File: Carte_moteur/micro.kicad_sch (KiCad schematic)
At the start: 27 parts, among them U501 STM32G474RETx

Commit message: updated motor PCB
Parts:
- removed C501, C507: C, Capacitor_SMD:C_0603_1608Metric_Pad1.08x0.95mm_HandSolder, symbol Device:C
- removed C502: C, Capacitor_SMD:C_0805_2012Metric_Pad1.18x1.45mm_HandSolder, symbol Device:C
- removed R501, R502, R503, R504, R505, R506, R507, R508, R509: R_US, Resistor_SMD:R_0603_1608Metric_Pad0.98x0.95mm_HandSolder, symbol Device:R_US
- added C508: C, Capacitor_SMD:C_0603_1608Metric_Pad1.08x0.95mm_HandSolder, symbol Device:C
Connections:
- net DIR1: now also U501.41 (PC9); no longer U501.43 (PA9)
- net DIR2: now also U501.37 (PB15); no longer U501.45 (PA11)
- net DIR3: now also U501.45 (PA11); no longer U501.41 (PC9)
- net ENC1_A: now also U501.12 (PA0); no longer U501.8 (PC0)
- net ENC1_B: now also U501.13 (PA1); no longer U501.9 (PC1)
- net ENC1_I: now also U501.34 (PB12); no longer U501.46 (PA12)
- net ENC2_A: now also U501.8 (PC0); no longer U501.38 (PC6)
- net ENC2_B: now also U501.9 (PC1); no longer U501.18 (PA4)
- net ENC2_I: now also U501.46 (PA12); no longer U501.55 (PD2)
- net ENC3_A: now also U501.38 (PC6); no longer U501.12 (PA0)
- net ENC3_B: now also U501.18 (PA4); no longer U501.13 (PA1)
- net ENC3_I: now also U501.55 (PD2); no longer U501.34 (PB12)
- net GND: now also C508.1
- net STEP1: now also U501.40 (PC8); no longer U501.42 (PA8)
- net STEP2: now also U501.36 (PB14); no longer U501.44 (PA10)
- net STEP3: now also U501.44 (PA10); no longer U501.40 (PC8)
- net TMC1: now also R514.1, R515.1; no longer R512.1, R513.1
- net TMC2: now also R512.1, R513.1; no longer R516.1, R517.1
- net TMC3: now also R516.1, R517.1; no longer R514.1, R515.1
- net UART3_TX: now also U501.62 (PB9); no longer U501.30 (PB10)
- net at R511.1, U501.28 (VREF+): now also C508.2
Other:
- moved on the sheet: R512, R513, R514, R515, R516, R517

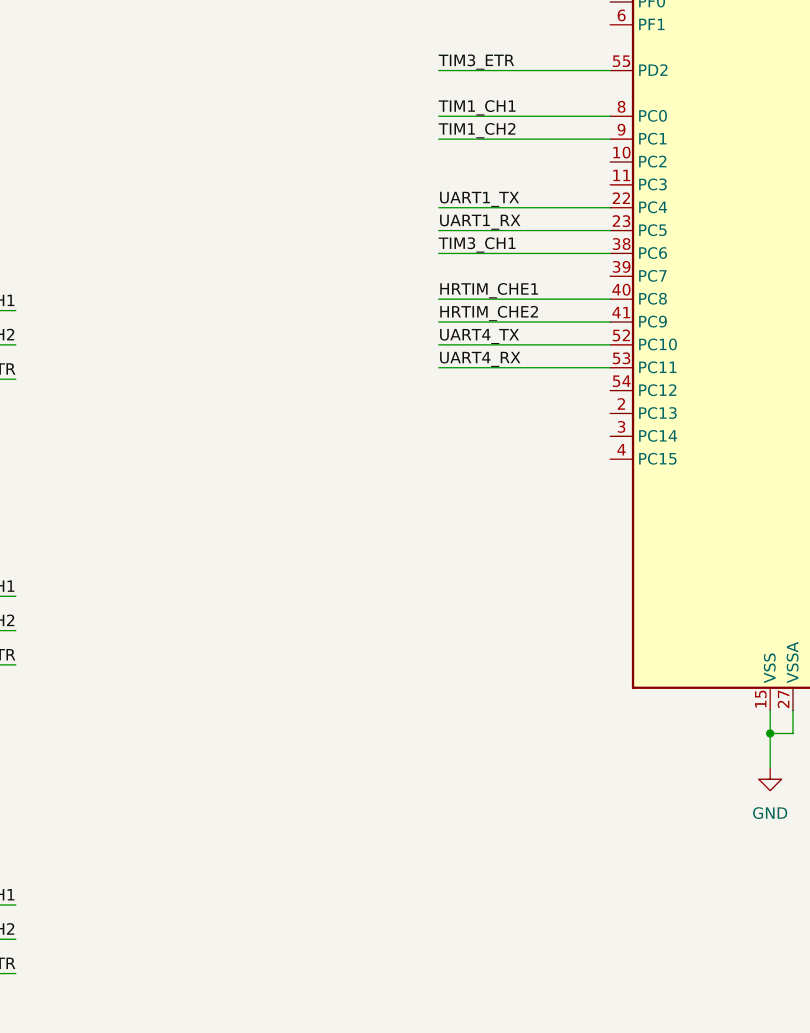
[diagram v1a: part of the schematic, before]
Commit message: debug led added. Modified power connector
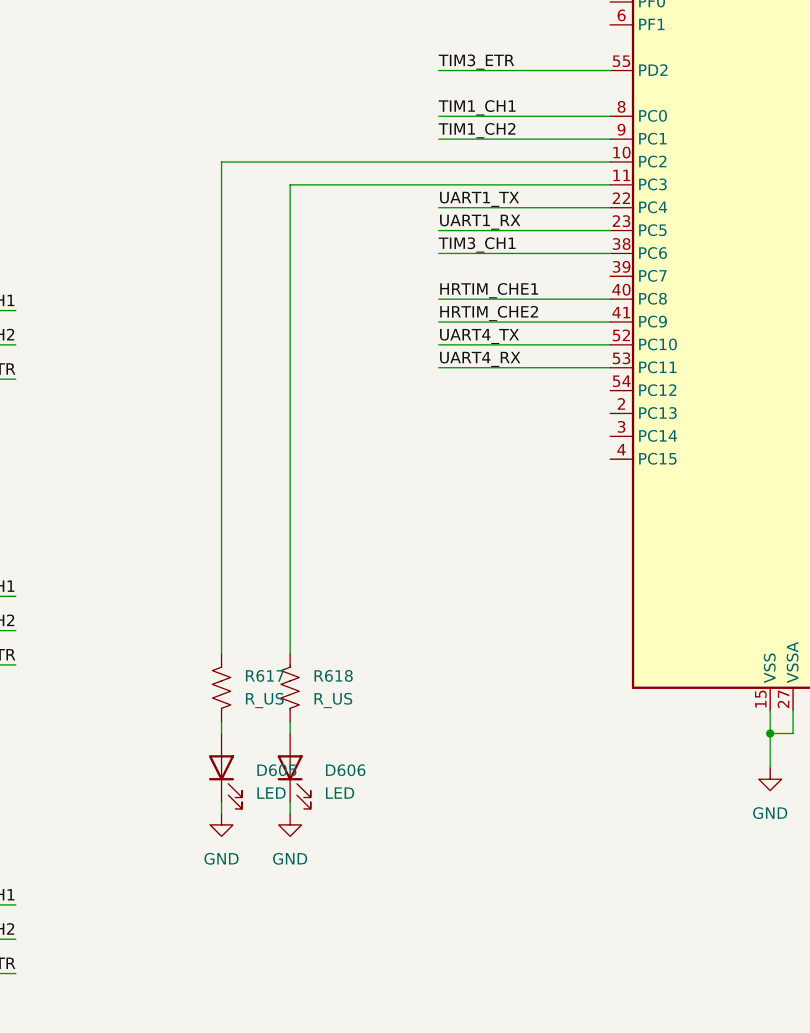
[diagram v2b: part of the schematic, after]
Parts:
- added D605, D606: LED, LED_SMD:LED_0805_2012Metric_Pad1.15x1.40mm_HandSolder, symbol Device:LED
- added R617, R618: R_US, Resistor_SMD:R_0603_1608Metric_Pad0.98x0.95mm_HandSolder, symbol Device:R_US
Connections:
- net GND: now also D605.1 (K), D606.1 (K)
- net at U501.10 (PC2): now also R617.1
- net at U501.11 (PC3): now also R618.1
- new net: D606.2 (A), R618.2
- new net: D605.2 (A), R617.2

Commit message: changed pwr connector
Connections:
- no-connect marks 0 -> 17
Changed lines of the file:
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@@
 		(color 0 0 0 0)
+	)
+	(no_connect
+		(at 120.65 54.61)
+	)
+	(no_connect
+		(at 120.65 95.25)
+	)
+	(no_connect
+		(at 120.65 102.87)
+	)
+	(no_connect
+		(at 120.65 82.55)
+	)
+	(no_connect
+		(at 156.21 87.63)
+	)
+	(no_connect
+		(at 120.65 97.79)
+	)
+	(no_connect
+		(at 156.21 90.17)
+	)
+	(no_connect
+		(at 156.21 64.77)
+	)
+	(no_connect
+		(at 156.21 100.33)
+	)
+	(no_connect
+		(at 156.21 118.11)
+	)
+	(no_connect
+		(at 156.21 110.49)
+	)
+	(no_connect
+		(at 156.21 62.23)
+	)
+	(no_connect
+		(at 156.21 97.79)
+	)
+	(no_connect
+		(at 120.65 52.07)
+	)
+	(no_connect
+		(at 156.21 102.87)
+	)
+	(no_connect
+		(at 120.65 100.33)
+	)
+	(no_connect
+		(at 156.21 85.09)
 	)
 	(wire

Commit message: update motor board values
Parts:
- C503, C504, C505, C506: value C -> 100nF
- C508: value C -> 10uF
- R510: value R_US -> 10k
- R511: value R_US -> 100R
- R512, R513, R514, R515, R516, R517, R617, R618: value R_US -> 1k
- R518: value R_US -> 10R
- R519: value R_US -> 10K
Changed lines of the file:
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@@
 			)
 		)
-		(property "Value" "C"
+		(property "Value" "100nF"
 			(at 132.08 179.0699 0)
 			(effects
@@
 			)
 		)
-		(property "Value" "C"
+		(property "Value" "100nF"
 			(at 146.05 179.0699 0)
 			(effects
@@
 			)
 		)
-		(property "Value" "R_US"
+		(property "Value" "1k"
 			(at 236.22 58.42 90)
 			(effects
@@
 			)
 		)
-		(property "Value" "R_US"
+		(property "Value" "1k"
 			(at 87.63 129.5399 0)
 			(effects
@@
 			)
 		)
-		(property "Value" "R_US"
+		(property "Value" "1k"
 			(at 80.01 129.5399 0)
 			(effects
@@
 			)
 		)
-		(property "Value" "R_US"
+		(property "Value" "10k"
 			(at 85.09 35.5599 0)
 			(effects
@@
 			)
 		)
-		(property "Value" "C"
+		(property "Value" "10uF"
 			(at 104.1399 38.1 0)
 			(effects
@@
 			)
 		)
-		(property "Value" "C"
+		(property "Value" "100nF"
 			(at 106.68 179.0699 0)
 			(effects
@@
 			)
 		)
-		(property "Value" "R_US"
+		(property "Value" "1k"
 			(at 236.22 35.56 90)
 			(effects
@@
 			)
 		)
-		(property "Value" "R_US"
+		(property "Value" "1k"
 			(at 236.22 80.01 90)
 			(effects
@@
 			)
 		)
-		(property "Value" "R_US"
+		(property "Value" "10R"
 			(at 260.35 43.1799 0)
 			(effects
@@
 			)
 		)
-		(property "Value" "R_US"
+		(property "Value" "10K"
 			(at 260.35 66.0399 0)
 			(effects
@@
 			)
 		)
-		(property "Value" "C"
+		(property "Value" "100nF"
 			(at 119.38 179.0699 0)
 			(effects
@@
 			)
 		)
-		(property "Value" "R_US"
+		(property "Value" "100R"
 			(at 113.03 35.5599 0)
 			(effects
@@
 			)
 		)
-		(property "Value" "R_US"
+		(property "Value" "1k"
 			(at 236.22 71.12 90)
 			(effects
@@
 			)
 		)
-		(property "Value" "R_US"
+		(property "Value" "1k"
 			(at 236.22 26.67 90)
 			(effects
@@
 			)
 		)
-		(property "Value" "R_US"
+		(property "Value" "1k"
 			(at 236.22 48.26 90)
 			(effects
